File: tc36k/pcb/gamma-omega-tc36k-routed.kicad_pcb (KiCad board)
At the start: 2 copper layers, 232.8 x 111.4 mm, 45 parts

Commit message: Add text to board silkscreen with date & tools
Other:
- board text added: "Designed Tokyo June 2025, with Ergogen v4.1.0 & KiCad v9.0.2"
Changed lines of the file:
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@@
+		)
+	)
+	(gr_text "Designed Tokyo June 2025, with \nErgogen v4.1.0 & KiCad v9.0.2"
+		(at 45.91 114.2 0)
+		(layer "F.SilkS")
+		(effects
+			(font
+				(size 1.4 1.4)
+				(thickness 0.1875)
+			)
+			(justify left bottom)
 		)
 	)
@@
 		)
 	)
+	(gr_text "Designed Tokyo June 2025, with \nErgogen v4.1.0 & KiCad v9.0.2"
+		(at 267.46 114.2 0)
+		(layer "B.SilkS")
+		(effects
+			(font
+				(size 1.4 1.4)
+				(thickness 0.1875)
+			)
+			(justify left bottom mirror)
+		)
+	)

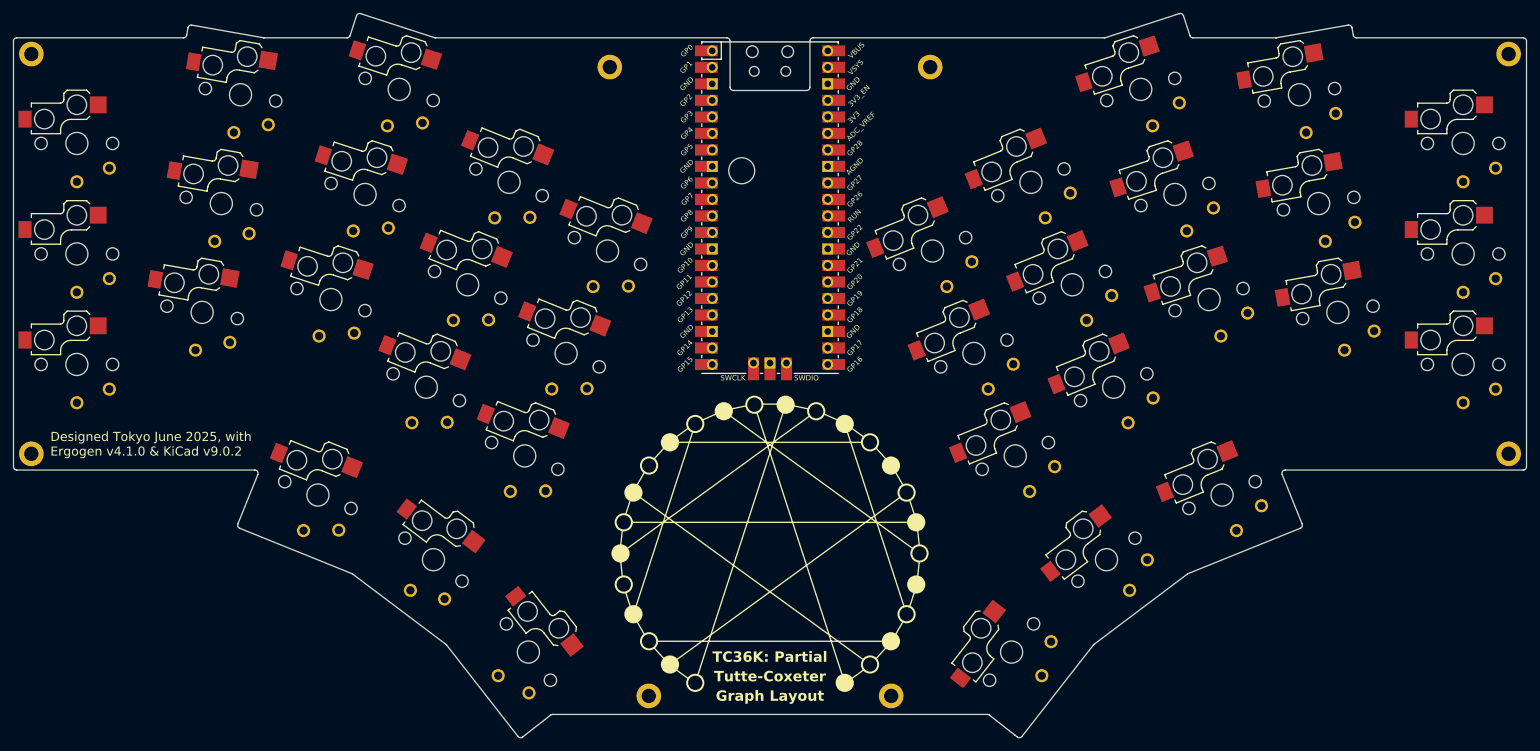
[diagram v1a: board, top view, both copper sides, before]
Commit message: Traces and ground plane in KiCad v9.0.2
This was the result of a lot of iterative work, which does not
work well in version control (too much floating point noise).

This passes the Design Rules Checker except for a warning from
each ceoloide footprint not being in the library, a warning for
the USB cut-out clipping the controller footprint (deliberate),
and 2 errors about not enough spokes for ground plane zones
(cofigurable threshold).
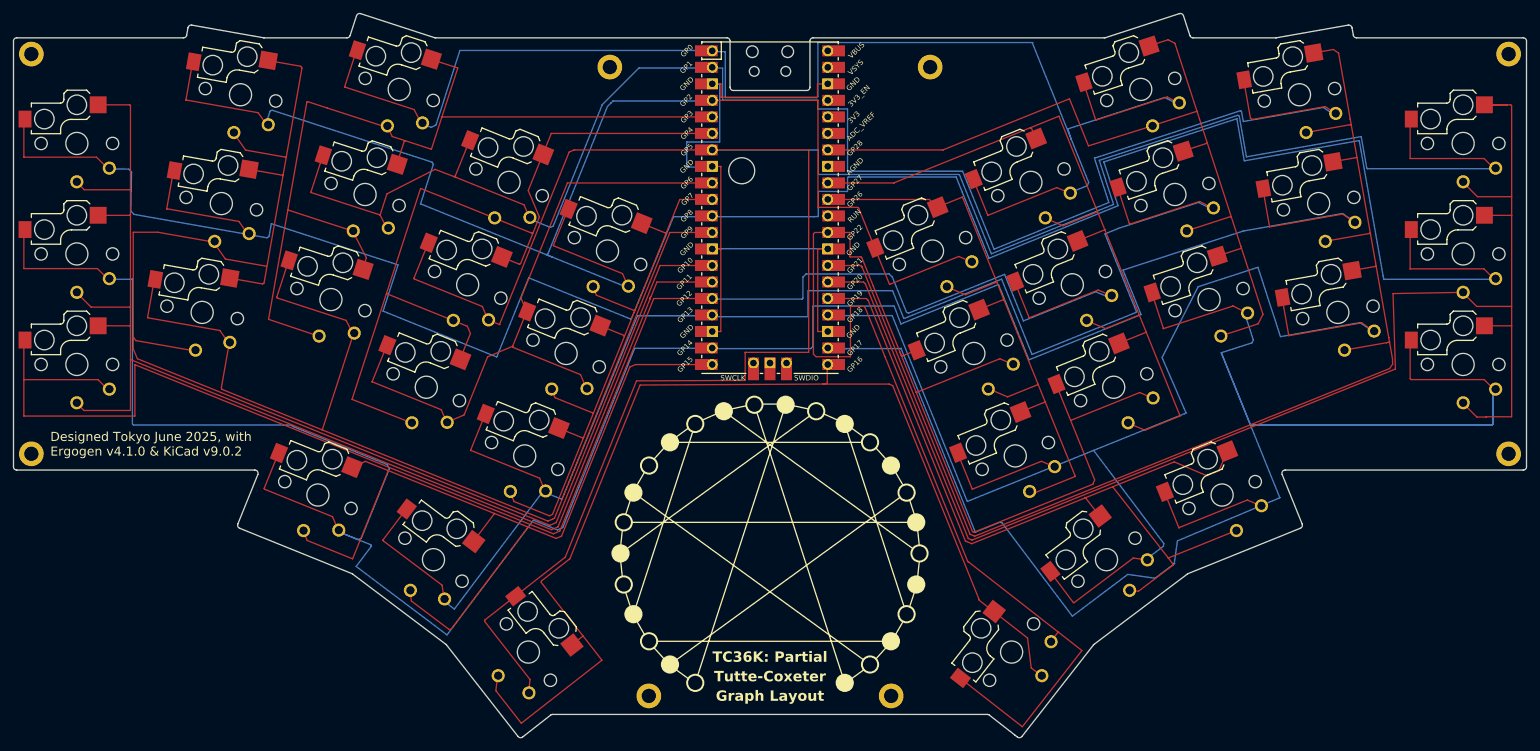
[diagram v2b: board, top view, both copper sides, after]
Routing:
- net R13: track 0.00 -> 381.6 mm
- net R10: track 0.00 -> 367.1 mm
- net R2: track 0.00 -> 363.1 mm
- net R12: track 0.00 -> 297.3 mm
- net R1: track 0.00 -> 263.3 mm
- net R7: track 0.00 -> 253.9 mm
- net R4: track 0.00 -> 251.5 mm
- net R9: track 0.00 -> 241.8 mm
- net C12: track 0.00 -> 231.2 mm
- net C2: track 0.00 -> 231.2 mm
- net R8: track 0.00 -> 224.1 mm
- net R6: track 0.00 -> 215.7 mm
- net R11: track 0.00 -> 215.6 mm
- net C1: track 0.00 -> 209.2 mm
- net C10: track 0.00 -> 202.1 mm
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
